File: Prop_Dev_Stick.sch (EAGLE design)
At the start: 55 parts, among them J1 MF-CON-MICROUSB-RIGHT, J3 M20-7822046, J4 M20-7822046, J5 M20-7820442, J6 M20-7820442, U1 P8X32A-Q44, U2 FT230XQ-R, U3 TPS2113ADRBR, U4 CAT24C512WI-GT3, U5 MAX11613EUA+, U6 NCP1117LPST33T3G, U7 IRLML6401TRPBF, X1 ABMM-6.000MHZ-B2-T

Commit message: Updated design to use latest library style!
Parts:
- removed J6: M20-7820442, PP_Connectors:PH_1X04HEADER_PTH_ROUND
- added J2: (no value), PP_Connectors:CON_01X04_2.54MM_PIN_HEADER
- C1, C10, C11, C12, C13, C14, C15, C16, C2, C3, C4, C5, C6, C7: device PP_Passives:CAPACITOR_NON_POLAR0603 -> PP_Passives:CAPACITOR_NON_POLAR_0603
- J1: device MF_Connectors:USB_CON_5PRIGHT -> PP_Connectors:USB_5PIN_10118193-0001LF
- J3: value M20-7822046 -> (none); device PP_Connectors:PH_1X20HEADER_01X20_PTH_ROUND -> PP_Connectors:CON_01X04_2.54MM_PIN_HEADER
- J4: device PP_Connectors:PH_1X20HEADER_01X20_PTH_ROUND -> PP_Connectors:CON_01X20_2.54MM_PIN_HEADER
- J5: value M20-7820442 -> M20-7822046; device PP_Connectors:PH_1X04HEADER_PTH_ROUND -> PP_Connectors:CON_01X20_2.54MM_PIN_HEADER
- L1: device PP_Passives:INDUCTOR0603 -> PP_Passives:INDUCTOR_0603
- PWR, TX/RX: device PP_LED:LED_SINGLE0805 -> PP_LED:LED_SINGLE_0805
- R1, R10, R11, R12, R13, R14, R15, R16, R17, R18, R2, R3, R4, R5, R6, R7, R8, R9: device PP_Passives:RESISTOR0603 -> PP_Passives:RESISTOR_0603
- U1: device PP_DigitalIC:P8X32A_PROPELLERLQFP-44 -> PP_DigitalIC:P8X32A-Q44
- U2: device PP_DigitalIC:FT230XQFN-16 -> PP_DigitalIC:FT230XQ
- U3: device PP_PowerIC:TPS2111SON-8 -> PP_PowerIC:TPS211(2/3)ADR
- U4: device PP_DigitalIC:CAT24M01XI-T2SOIC-8_W -> PP_DigitalIC:EEPROM_I2CSOIC-8_W
- U7: device PP_DiscreteSemi:MOSFET_P-CHANNEL_SINGLESOT-23 -> PP_DiscreteSemi:MOSFET_P-CHANNEL_SINGLE_SOT-23
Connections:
- net 3.3V: now also J2.2, J3.2, J5.3; no longer J3.3, J5.2, J6.2
- net A0: now also J2.3; no longer J6.3
- net A1: now also J2.4; no longer J6.4
- net A2: now also J3.3; no longer J5.3
- net A3: now also J3.4; no longer J5.4
- net GND: now also J2.1, J3.1, J5.4, U1.!BOE, U3.!EN, U4.A0; no longer J3.4, J5.1, J6.1, U1.BOE', U3.D1
- net P10: now also J4.15; no longer J3.15
- net P11: now also J4.16; no longer J3.16
- net P12: now also J4.17; no longer J3.17
- net P13: now also J4.18; no longer J3.18
- net P14: now also J4.19; no longer J3.19
- net P15: now also J4.20; no longer J3.20
- net P16: now also J5.20; no longer J4.20
- net P17: now also J5.19; no longer J4.19
- net P18: now also J5.18; no longer J4.18
- net P19: now also J5.17; no longer J4.17
- net P20: now also J5.16; no longer J4.16
- net P21: now also J5.15; no longer J4.15
- net P22: now also J5.14; no longer J4.14
- net P23: now also J5.13; no longer J4.13
- net P24: now also J5.12; no longer J4.12
- net P25: now also J5.11; no longer J4.11
- net P26: now also J5.10; no longer J4.10
- net P27: now also J5.9; no longer J4.9
- net P4: now also J4.9; no longer J3.9
- net P5: now also J4.10; no longer J3.10
- net P6: now also J4.11; no longer J3.11
- net P7: now also J4.12; no longer J3.12
- net P8: now also J4.13; no longer J3.13
- net P9: now also J4.14; no longer J3.14
- net RES: now also U1.!RES; no longer U1.RES'
- net RX: now also J5.6; no longer J4.6
- net SCL: now also J5.8; no longer J4.8
- net SDA: now also J5.7; no longer J4.7
- net SD_CS: now also J4.5; no longer J3.5
- net SD_DI: now also J4.6; no longer J3.6
- net SD_DO: now also J4.8; no longer J3.8
- net SD_SCLK: now also J4.7; no longer J3.7
- net TX: now also J5.5; no longer J4.5
- net VBUS_P2: now also J5.2; no longer J3.2
- net VIN: now also J5.1; no longer J3.1
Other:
- moved on the sheet: C1, C10, C11, C12, C13, C14, C15, C16, C2, C3, C4, C5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

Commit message: Updated to REV 4B
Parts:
- U$1: REVNUM REV 4 -> REV 4B
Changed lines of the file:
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@@
 <attribute name="DNAME" value="Parker Dillmann"/>
 <attribute name="PNAME" value="Propeller Dev Stick"/>
-<attribute name="REVNUM" value="REV 4"/>
+<attribute name="REVNUM" value="REV 4B"/>
 </part>
 <part name="U2" library="PP_DigitalIC" deviceset="FT230X" device="Q" value="FT230XQ-R"/>

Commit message: REV 4B
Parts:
- J1: device PP_Connectors:USB_5PIN_10118193-0001LF -> MF_Connectors:USB_MICRO_RIGHT
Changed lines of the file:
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@@
 <layer number="122" name="_bsilk" color="7" fill="1" visible="no" active="yes"/>
 <layer number="125" name="_tNames" color="7" fill="1" visible="no" active="yes"/>
+<layer number="128" name="128bmp" color="1" fill="10" visible="yes" active="yes"/>
+<layer number="129" name="129bmp" color="2" fill="4" visible="yes" active="yes"/>
+<layer number="130" name="130bmp" color="2" fill="1" visible="yes" active="yes"/>
 <layer number="131" name="prix" color="7" fill="1" visible="yes" active="yes"/>
 <layer number="132" name="test" color="7" fill="1" visible="yes" active="yes"/>
@@
 <part name="R18" library="PP_Passives" deviceset="RESISTOR" device="_0603" value="25K"/>
 <part name="SD1" library="MF_Connectors" deviceset="SD_CARD_SLOT" device="_MICRO_RIGHT" value="MF-CON-MICROSDSLOT-RIGHT"/>
-<part name="J1" library="PP_Connectors" deviceset="USB_5PIN" device="_10118193-0001LF" value="MF-CON-MICROUSB-RIGHT"/>
 <part name="X1" library="MF_Frequency_Control" deviceset="XTL" device="_7MMX5MM" value="ABMM-6.000MHZ-B2-T"/>
 <part name="RESET" library="MF_Switches" deviceset="TACT" device="_4.2MM" value="MF-SW-TACT-4.2MM"/>
@@
 <part name="J4" library="PP_Connectors" deviceset="CON_01X20" device="_2.54MM_PIN_HEADER" value="M20-7822046"/>
 <part name="J5" library="PP_Connectors" deviceset="CON_01X20" device="_2.54MM_PIN_HEADER" value="M20-7822046"/>
+<part name="J1" library="MF_Connectors" deviceset="USB" device="_MICRO_RIGHT" value="MF-CON-MICROUSB-RIGHT"/>
 </parts>
 <sheets>
@@
 <instance part="R18" gate="G$1" x="-76.2" y="185.42" rot="R90"/>
 <instance part="SD1" gate="G$1" x="-231.14" y="177.8" rot="MR180"/>
-<instance part="J1" gate="G$1" x="-386.08" y="259.08"/>
 <instance part="X1" gate="G$1" x="-144.78" y="254" smashed="yes" rot="R180">
 <attribute name="NAME" x="-142.24" y="259.08" size="0.8128" layer="95" font="vector" align="top-left"/>
@@
 <instance part="J4" gate="G$1" x="-127" y="254"/>
 <instance part="J5" gate="G$1" x="-101.6" y="254"/>
+<instance part="J1" gate="G$1" x="-381" y="251.46"/>
 </instances>
 <busses>
@@
 <wire x1="-373.38" y1="246.38" x2="-370.84" y2="246.38" width="0.1524" layer="91"/>
 <label x="-368.3" y="246.38" size="0.8128" layer="95" font="vector"/>
-<pinref part="J1" gate="G$1" pin="GND"/>
-<pinref part="J1" gate="G$1" pin="SLD"/>
 <wire x1="-370.84" y1="246.38" x2="-365.76" y2="246.38" width="0.1524" layer="91"/>
 <wire x1="-373.38" y1="243.84" x2="-370.84" y2="243.84" width="0.1524" layer="91"/>
 <wire x1="-370.84" y1="243.84" x2="-370.84" y2="246.38" width="0.1524" layer="91"/>
 <junction x="-370.84" y="246.38"/>
+<pinref part="J1" gate="G$1" pin="GND"/>
+<pinref part="J1" gate="G$1" pin="SLD"/>
 </segment>
 <segment>

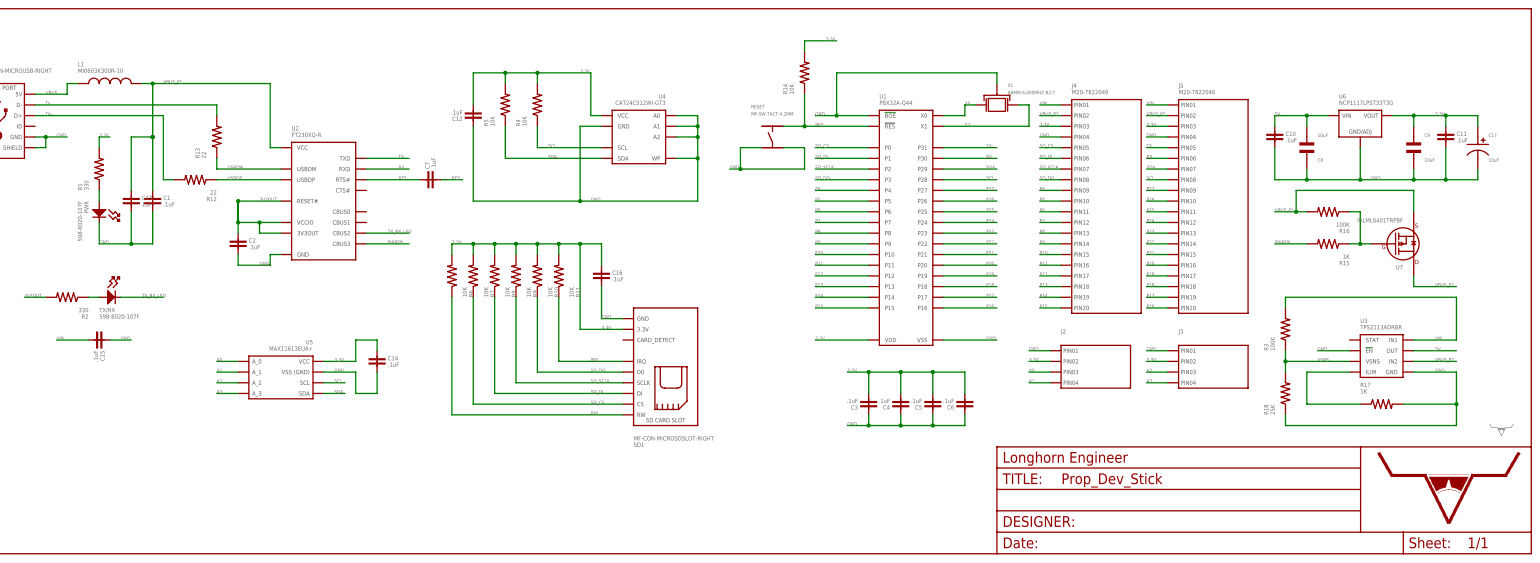
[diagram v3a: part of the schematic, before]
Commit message: Working on REV5
REV5 will feature 0402 parts, QFN Prop, USB Type-C, and a host of other
small changes.
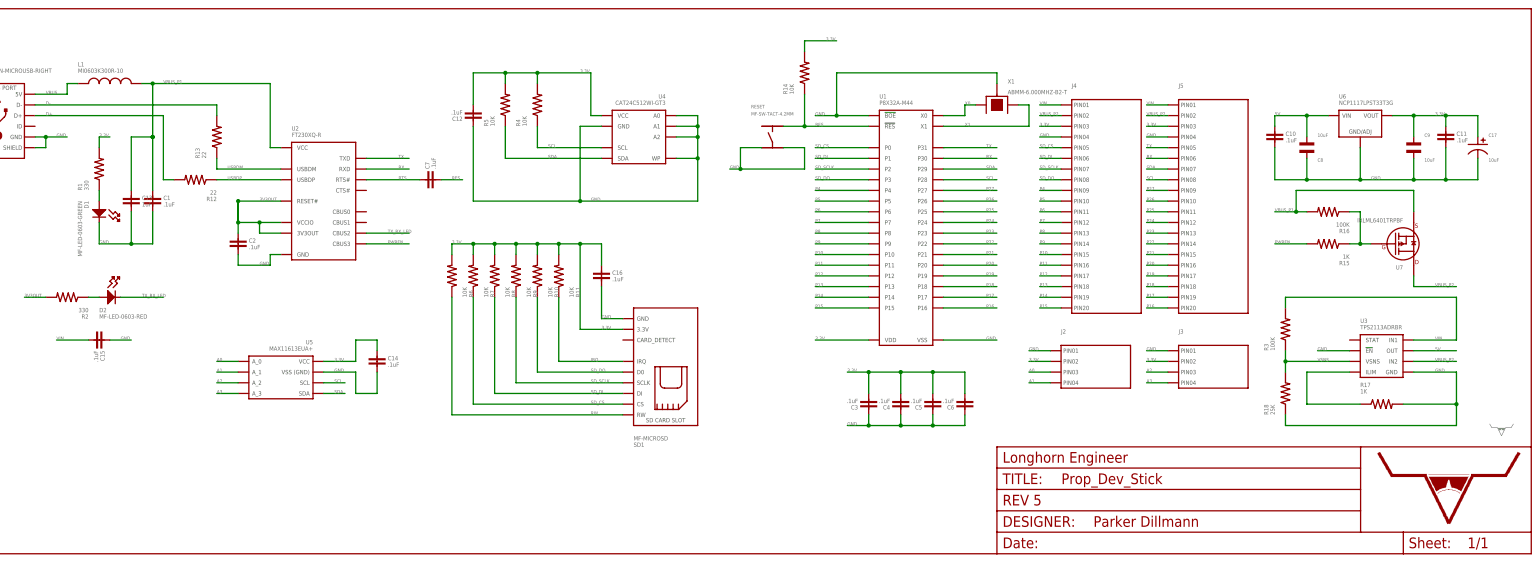
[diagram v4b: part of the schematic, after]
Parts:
- removed PWR, TX/RX: 598-8020-107F, PP_LED:LED_SINGLE_0805
- added D1: MF-LED-0603-GREEN, MF_LEDs:LED_SINGLE-0603-GREEN
- added D2: MF-LED-0603-RED, MF_LEDs:LED_SINGLE-0603-RED
- C1, C10, C11, C12, C13, C14, C15, C16, C2, C3, C4, C5, C6, C7: device PP_Passives:CAPACITOR_NON_POLAR_0603 -> PP_Passives:CAPACITOR_NON_POLAR_0402
- J4, J5: value M20-7822046 -> (none)
- R1, R10, R11, R12, R13, R14, R15, R16, R17, R18, R2, R3, R4, R5, R6, R7, R8, R9: device PP_Passives:RESISTOR_0603 -> PP_Passives:RESISTOR_0402
- SD1: value MF-CON-MICROSDSLOT-RIGHT -> MF-MICROSD
- U$1: REVNUM REV 4B -> REV 5
- U1: value P8X32A-Q44 -> P8X32A-M44; device PP_DigitalIC:P8X32A-Q44 -> PP_DigitalIC:P8X32A-M44
- X1: device MF_Frequency_Control:XTL_7MMX5MM -> PP_FreqCtrl:SHIELDED_CRYSTAL_7MM_X_5MM
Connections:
- net GND: now also D1.CATHODE, X1.P$3; no longer PWR.CATHODE, X1.GND
- net N$1: now also D1.ANODE; no longer PWR.ANODE
- net N$2: now also D2.ANODE; no longer TX/RX.ANODE
- net TX_RX_LED: now also D2.CATHODE; no longer TX/RX.CATHODE
- net X0: now also X1.P$2; no longer X1.X1
- net X1: now also X1.P$1; no longer X1.X0

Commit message: pushing updates from long ago
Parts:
- removed C10, C11, C12, C14, C15, C16, C6, C7: .1uF, PP_Passives:CAPACITOR_NON_POLAR_0402
- removed C13: 1uF, PP_Passives:CAPACITOR_NON_POLAR_0402
- removed C17: 10uF, MF_Passives:CAPACITOR_P_4MM
- removed D1: MF-LED-0603-GREEN, MF_LEDs:LED_SINGLE-0603-GREEN
- removed D2: MF-LED-0603-RED, MF_LEDs:LED_SINGLE-0603-RED
- removed L1: MI0603K300R-10, PP_Passives:INDUCTOR_0603
- removed R1, R2: 330, PP_Passives:RESISTOR_0402
- removed R10, R11, R14: 10K, PP_Passives:RESISTOR_0402
- removed R12: 22, PP_Passives:RESISTOR_0402
- removed R17: 1K, PP_Passives:RESISTOR_0402
- removed R18: 25K, PP_Passives:RESISTOR_0402
- removed R3: 100K, PP_Passives:RESISTOR_0402
- removed RESET: MF-SW-TACT-4.2MM, MF_Switches:TACT_4.2MM
- removed U6: NCP1117LPST33T3G, MF_IC_Power:NCP1117LPST33T3G
- removed X1: ABMM-6.000MHZ-B2-T, PP_FreqCtrl:SHIELDED_CRYSTAL_7MM_X_5MM
- added C18, C19: 0.1uF, MF_Passives:CAPACITOR_NP_0603
- added C20: 1uF, MF_Passives:CAPACITOR_NP_0603
- added C21, C22: 47pF, MF_Passives:CAPACITOR_NP_0603
- added C24, C25, C27, C28, C29: 0.1uF, MF_Passives:CAPACITOR_NP_0402
- added L3, L4: MI0603K300R-10, MF_Passives:INDUCTOR_0603
- added PWR, TXRX1: MF-LED-0603-RED, MF_LEDs:LED_SINGLE-0603-RED
- added R24: 5.1K, MF_Passives:RESISTOR_0603
- added R25, R26: 27, MF_Passives:RESISTOR_0603
- added R29, R31: 330, MF_Passives:RESISTOR_0402
- added U8: CAT24C512WI-GT3, PP_DigitalIC:EEPROM_I2CSOIC-8_W
- added X3: ABMM-6.000MHZ-B2-T, MF_Frequency_Control:CYRSTAL_GND_ABMM
- C1, C2, C3, C4: value .1uF -> 0.1uF; device PP_Passives:CAPACITOR_NON_POLAR_0402 -> MF_Passives:CAPACITOR_NP_0603
- C5: value .1uF -> 0.1uF; device PP_Passives:CAPACITOR_NON_POLAR_0402 -> MF_Passives:CAPACITOR_NP_0402; MPN (none) -> MF-CAP-0603-0.1uF
- J1: value MF-CON-MICROUSB-RIGHT -> (none); device MF_Connectors:USB_MICRO_RIGHT -> PP_Connectors:USB_TYPE-C_105450-0101
- J2: LABEL01 (none) -> GND; LABEL02 (none) -> 3.3V; LABEL03 (none) -> A0; LABEL04 (none) -> A1
- J3: LABEL01 (none) -> GND; LABEL02 (none) -> 3.3V; LABEL03 (none) -> A2; LABEL04 (none) -> A3
- J4: LABEL01 (none) -> VIN; LABEL02 (none) -> 5V; LABEL03 (none) -> 3.3V; LABEL04 (none) -> GND; LABEL05 (none) -> P0; LABEL06 (none) -> P1; LABEL07 (none) -> P2; LABEL08 (none) -> P3; LABEL09 (none) -> P4; LABEL10 (none) -> P5; LABEL11 (none) -> P6; LABEL12 (none) -> P7; LABEL13 (none) -> P8; LABEL14 (none) -> P9; LABEL15 (none) -> P10; LABEL16 (none) -> P11; LABEL17 (none) -> P12; LABEL18 (none) -> P13; LABEL19 (none) -> P14; LABEL20 (none) -> P15
- J5: LABEL01 (none) -> VIN; LABEL02 (none) -> 5V; LABEL03 (none) -> 3.3V; LABEL04 (none) -> GND; LABEL05 (none) -> P31; LABEL06 (none) -> P30; LABEL07 (none) -> P29; LABEL08 (none) -> P28; LABEL09 (none) -> P27; LABEL10 (none) -> P26; LABEL11 (none) -> P25; LABEL12 (none) -> P24; LABEL13 (none) -> P23; LABEL14 (none) -> P22; LABEL15 (none) -> P21; LABEL16 (none) -> P20; LABEL17 (none) -> P19; LABEL18 (none) -> P18; LABEL19 (none) -> P17; LABEL20 (none) -> P16
- R13: value 22 -> 10K; device PP_Passives:RESISTOR_0402 -> MF_Passives:RESISTOR_0402; MPN (none) -> MF-RES-0805-10K
- R15: value 1K -> 10K; device PP_Passives:RESISTOR_0402 -> MF_Passives:RESISTOR_0402; MPN (none) -> MF-RES-0603-10K
- R16: value 100K -> 10K; device PP_Passives:RESISTOR_0402 -> MF_Passives:RESISTOR_0402; MPN (none) -> MF-RES-0603-10K
- R4, R5, R6, R7, R8, R9: device PP_Passives:RESISTOR_0402 -> MF_Passives:RESISTOR_0603
- U1: value P8X32A-M44 -> AP7361C-33ER-13; device PP_DigitalIC:P8X32A-M44 -> PP_PowerIC:LINEAR_VOTLAGE_REGULATORS_ADP3338
- U2: value FT230XQ-R -> IP4234CZ6,125; device PP_DigitalIC:FT230XQ -> PP_Passives:IP4234CZ6
- U3: value TPS2113ADRBR -> BQ24165RGET; device PP_PowerIC:TPS211(2/3)ADR -> PP_PowerIC:BQ24165RGET
- U4: value CAT24C512WI-GT3 -> FT230XQ-R; device PP_DigitalIC:EEPROM_I2CSOIC-8_W -> PP_DigitalIC:FT230XQ
- U7: value IRLML6401TRPBF -> P8X32A-Q44; device PP_DiscreteSemi:MOSFET_P-CHANNEL_SINGLE_SOT-23 -> PP_DigitalIC:P8X32A-M44; MPN (none) -> P8X32A-Q44
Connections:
- removed net 3V3OUT: C2.1, R2.2, U2.3V3OUT, U2.RESET#, U2.VCCIO
- removed net N$41: R15.1, R16.1, U7.GATE
- removed net N$7: R17.1, U3.ILIM
- removed net PWREN: R15.2, U2.CBUS3
- removed net VBUS: J1.5V, L1.P$1
- removed net VBUS_P1: C1.1, C13.1, L1.P$2, R16.2, U2.VCC, U7.SOURCE
- removed net VBUS_P2: J4.2, J5.2, U3.IN2, U7.DRAIN
- removed net VSNS: R18.2, R3.1, U3.VSNS
- removed net X0: U1.X0, X1.P$2
- removed net X1: U1.X1, X1.P$1
- new net BCD_CHARGER: U4.CBUS0
- new net CC1/1: J1.CC1, J1.CC2, R24.P$1
- new net N$11: J1.SHLD, L4.P$1
- new net N$16: C21.P$1, R26.P$1, U2.I/O1A
- new net N$17: C22.P$1, R25.P$1, U2.I/O2A
- new net N$3: PWR.CATHODE, R31.P$1
- new net USB_VBUS: C18.P$1, C20.P$1, L3.P$2, TXRX1.ANODE, U2.VB
- new net USB_VBUS_PORT: J1.VBUS, L3.P$1
- new net X4: U7.X0, X3.X1
- new net X5: U7.X1, X3.X0
- net 3.3V: now also C1.P$1, C19.P$1, C2.P$1, C24.P$1, C25.P$1, C27.P$1, C28.P$1, C29.P$1, C4.P$1, R13.P$1, R15.P$1, R16.P$1, R4.P$2, R5.P$2, R6.P$2, R7.P$2, R8.P$2, R9.P$2, U1.OUT, U4.3V3OUT, U4.RESET#, U4.VCCIO, U7.VDD, U8.VCC; no longer C11.1, C12.2, C14.1, C16.1, C17.P$1, C3.2, C4.2, C5.2, C6.2, R1.2, R10.2, R11.2, R14.2, R4.2, R5.2, R6.2, R7.2, R8.2, R9.2, U1.VDD, U6.VOUT
- net 5V: now also C3.P$1, J4.2, J5.2, PWR.ANODE, U1.IN; no longer C10.1, U3.OUT, U6.VIN
- net D+: now also J1.D+1, J1.D+2, U2.I/O1B; no longer J1.D+, R12.2
- net D-: now also J1.D-1, J1.D-2, U2.I/O2B; no longer J1.D-, R13.2
- net GND: now also C1.P$2, C18.P$2, C19.P$2, C2.P$2, C20.P$2, C21.P$2, C22.P$2, C24.P$2, C25.P$2, C27.P$2, C28.P$2, C29.P$2, C3.P$2, C4.P$2, L4.P$2, R24.P$2, R31.P$2, U1.GND, U7.!BOE, U7.VSS, U8.A0, U8.A1, U8.A2, U8.GND, U8.WP, X3.GND; no longer C1.2, C10.2, C11.2, C12.1, C13.2, C14.2, C15.1, C16.2, C17.P$2, C2.2, C3.1, C4.1, C5.1, C6.1, D1.CATHODE, J1.SLD, R17.2, R18.1, RESET.P$3, RESET.P$4, U1.!BOE, U1.VSS, U3.!EN, U3.GND, U4.A0, U4.A1, U4.A2, U4.WP, U6.GND/ADJ, X1.P$3
- net IRQ: now also R9.P$1; no longer R11.1
- net N$1: now also U4.CBUS3; no longer D1.ANODE, R1.1
- net N$2: now also R29.P$1, TXRX1.CATHODE; no longer D2.ANODE, R2.1
- net P10: now also U7.P10; no longer U1.P10
- net P11: now also U7.P11; no longer U1.P11
- net P12: now also U7.P12; no longer U1.P12
- net P13: now also U7.P13; no longer U1.P13
- net P14: now also U7.P14; no longer U1.P14
- net P15: now also U7.P15; no longer U1.P15
- net P16: now also U7.P16; no longer U1.P16
- net P17: now also U7.P17; no longer U1.P17
- net P18: now also U7.P18; no longer U1.P18
- net P19: now also U7.P19; no longer U1.P19
- net P20: now also U7.P20; no longer U1.P20
- net P21: now also U7.P21; no longer U1.P21
- net P22: now also U7.P22; no longer U1.P22
- net P23: now also U7.P23; no longer U1.P23
- net P24: now also U7.P24; no longer U1.P24
- net P25: now also U7.P25; no longer U1.P25
- net P26: now also U7.P26; no longer U1.P26
- net P27: now also U7.P27; no longer U1.P27
- net P4: now also U7.P4; no longer U1.P4
- net P5: now also U7.P5; no longer U1.P5
- net P6: now also U7.P6; no longer U1.P6
- net P7: now also U7.P7; no longer U1.P7
- net P8: now also U7.P8; no longer U1.P8
- net P9: now also U7.P9; no longer U1.P9
- net RES: now also C5.P$1, R13.P$2, U7.!RES; no longer C7.2, R14.1, RESET.P$2, U1.!RES
- net RTS: now also C5.P$2, U4.RTS#; no longer C7.1, U2.RTS#
- net RW: now also R4.P$1; no longer R6.1
- net RX: now also U4.RXD, U7.P30; no longer U1.P30, U2.RXD
- net SCL: now also R16.P$2, U7.P28, U8.SCL; no longer R4.1, U1.P28, U4.SCL
- net SDA: now also R15.P$2, U7.P29, U8.SDA; no longer R5.1, U1.P29, U4.SDA
- net SD_CS: now also R5.P$1, U7.P0; no longer R7.1, U1.P0
- net SD_DI: now also R6.P$1, U7.P1; no longer R8.1, U1.P1
- net SD_DO: now also R8.P$1, U7.P3; no longer R10.1, U1.P3
- net SD_SCLK: now also R7.P$1, U7.P2; no longer R9.1, U1.P2
- net TX: now also U4.TXD, U7.P31; no longer U1.P31, U2.TXD
- net TX_RX_LED: now also R29.P$2, U4.CBUS2; no longer D2.CATHODE, U2.CBUS2
- net USBDM: now also R25.P$2, U4.USBDM; no longer R13.1, U2.USBDM
- net USBDP: now also R26.P$2, U4.USBDP; no longer R12.1, U2.USBDP
- net VIN: no longer C15.2, R3.2, U3.IN1
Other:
- moved on the sheet: C8, C9, J2, J3, J4, J5, R13, R15, R16, R4, R5, R6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
